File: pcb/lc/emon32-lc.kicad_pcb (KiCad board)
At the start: 4 copper layers, 55 x 40 mm, 93 parts, among them J1 AudioJack3_Ground_Switch, J2 AudioJack3_Ground_Switch, J3 Conn_02x05_Odd_Even, J4 RJ12, J5 Conn_Coaxial, J6 USB_C_Receptacle_USB2.0, J7 Conn_01x03_Male, J8 Conn_02x04_Odd_Even, J9 Conn_01x03_Male, SW1 SW_Push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

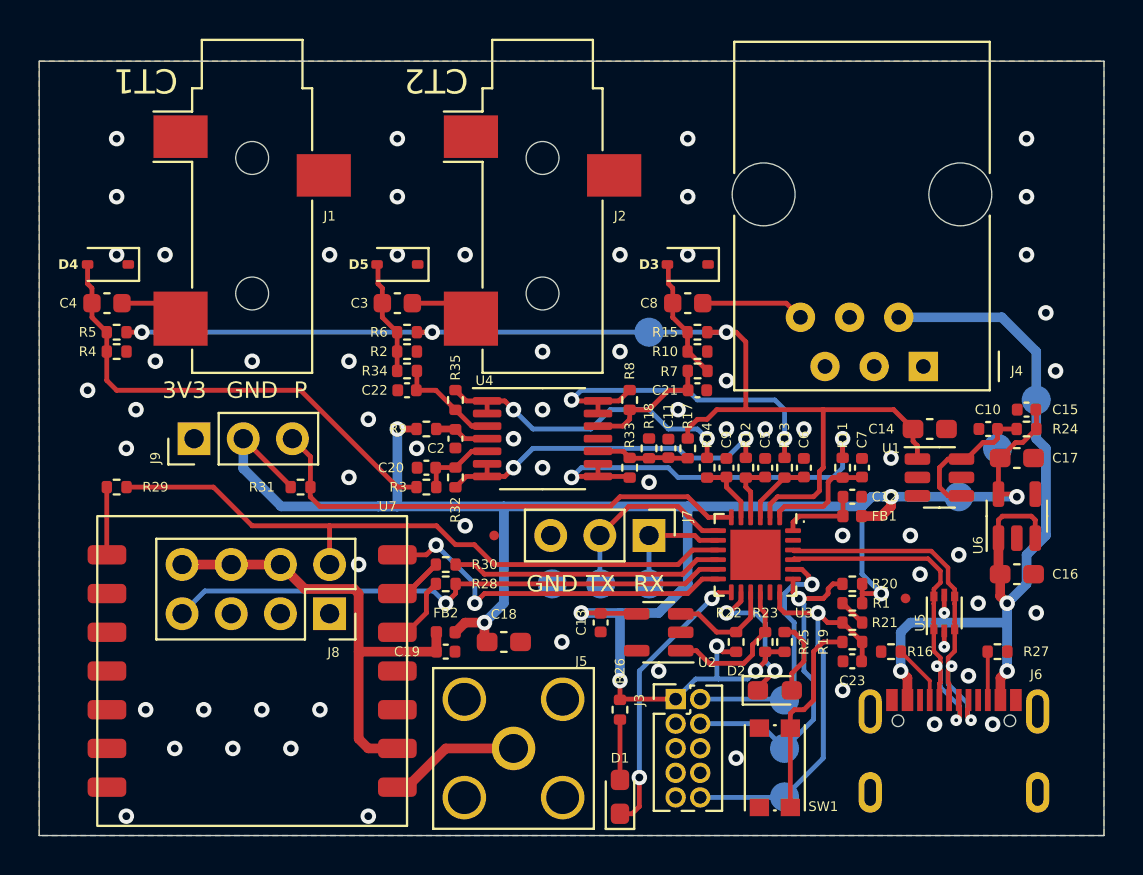
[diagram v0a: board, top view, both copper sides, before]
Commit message: * [LC]
  - Move ESP header out of RFM footprint to remove short risk
  - Remove all vias inside RFM footprint
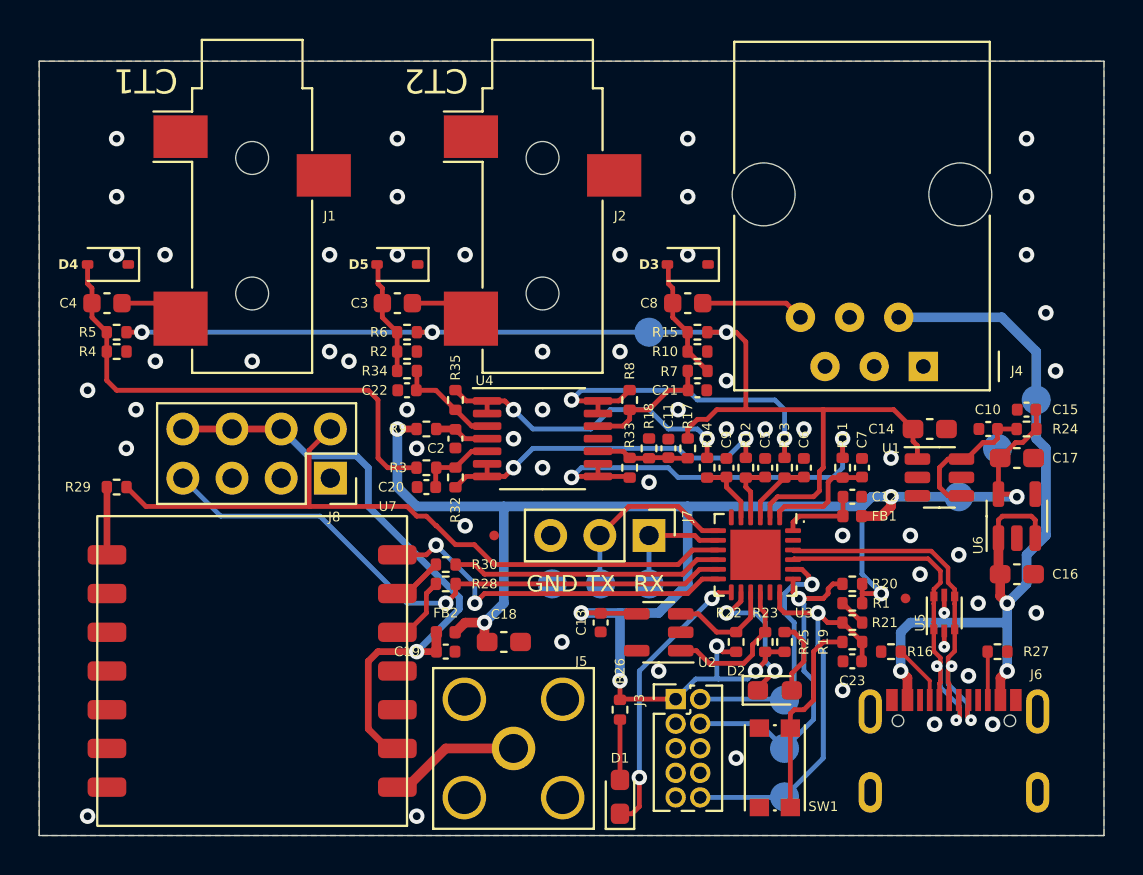
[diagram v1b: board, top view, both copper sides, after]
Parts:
- removed J9: Conn_01x03_Male, Connector_PinHeader_2.54mm:PinHeader_1x03_P2.54mm_Vertical
- removed R31: 3K3, Resistor_SMD:R_0402_1005Metric
- moved J8 7.00 mm to (130.0, 126.5)
- moved C20 1.00 mm to (135.0, 127.0)
- moved R3 1.00 mm to (135.0, 126.0)
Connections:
- U3 pad 6: /PULSE/DS18B20 -> unconnected-(U3-PA07-Pad6)
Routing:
- net /PULSE/DS18B20: track 26.0 -> 0.00 mm
- net +3V3: track 106.4 -> 91.0 mm
- net /3V3_TX: track 24.5 -> 32.4 mm, vias 0 -> 1
- net /MISO/UART_DATA_RX: track 34.5 -> 37.0 mm
- net /MOSI/UART_DATA_TX: track 29.4 -> 31.3 mm
- net Net-(D4-A2): track 24.7 -> 26.0 mm
- net GND: vias 64 -> 56
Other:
- board text removed: "P"

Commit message: * [LC]
  - Change to 8P8C header
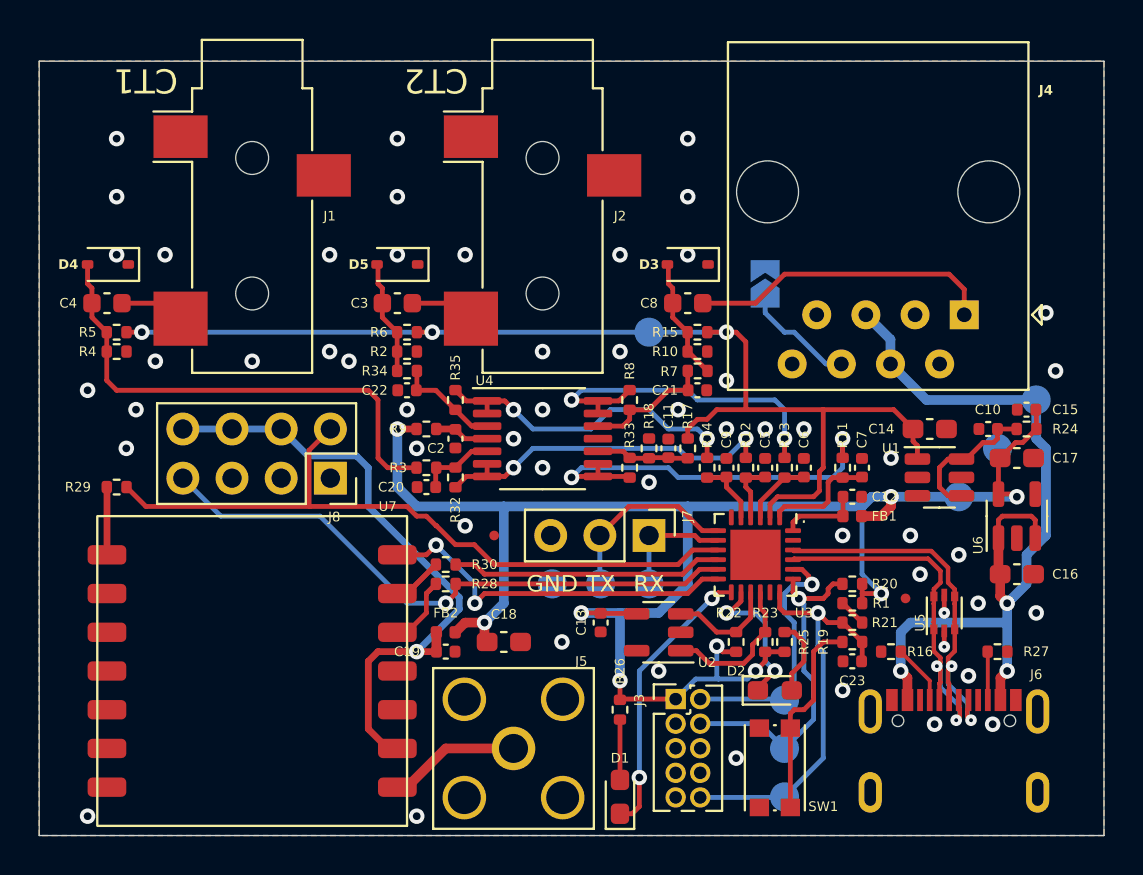
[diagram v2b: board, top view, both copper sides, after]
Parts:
- added JP1: Jumper_2_Open, Jumper:SolderJumper-2_P1.3mm_Open_TrianglePad1.0x1.5mm, B.Cu at (152.5, 116.5)
- J4: value RJ12 -> 8P8C; footprint Connector_RJ:RJ12_Amphenol_54601 -> Connector_RJ:RJ45_Amphenol_54602-x08_Horizontal
- moved J4 3.40 mm to (162.8, 118.1)
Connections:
- J4 pad 1: GND -> /V_AC_RAW0
- J4 pad 2: +5V -> unconnected-(J4-Pad2)
- J4 pad 4: unconnected-(J4-Pad4) -> +5V
- J4 pad 5: unconnected-(J4-Pad5) -> +5V
- J4 pad 6: /V_AC_RAW0 -> Net-(JP1-A)
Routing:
- net /V_AC_RAW0: track 5.35 -> 15.8 mm
- net Net-(JP1-A): track 0.00 -> 5.80 mm
- net +5V: track 45.2 -> 46.2 mm
- net GND: vias 56 -> 53
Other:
- board text added: "GND Link"
